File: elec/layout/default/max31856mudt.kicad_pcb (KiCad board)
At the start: 2 copper layers, 225.7 x 100.8 mm, 0 parts

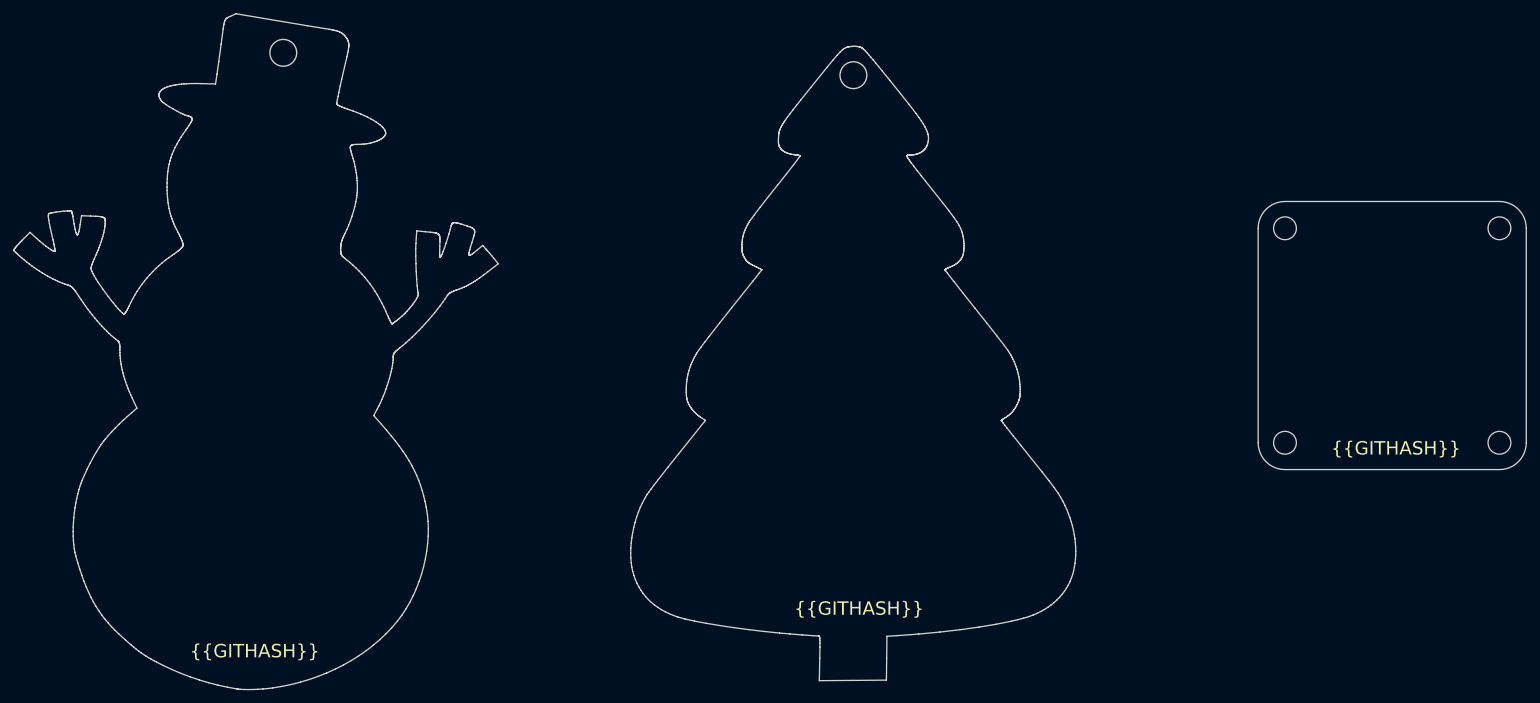
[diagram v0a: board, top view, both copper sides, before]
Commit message: added spi interfaces
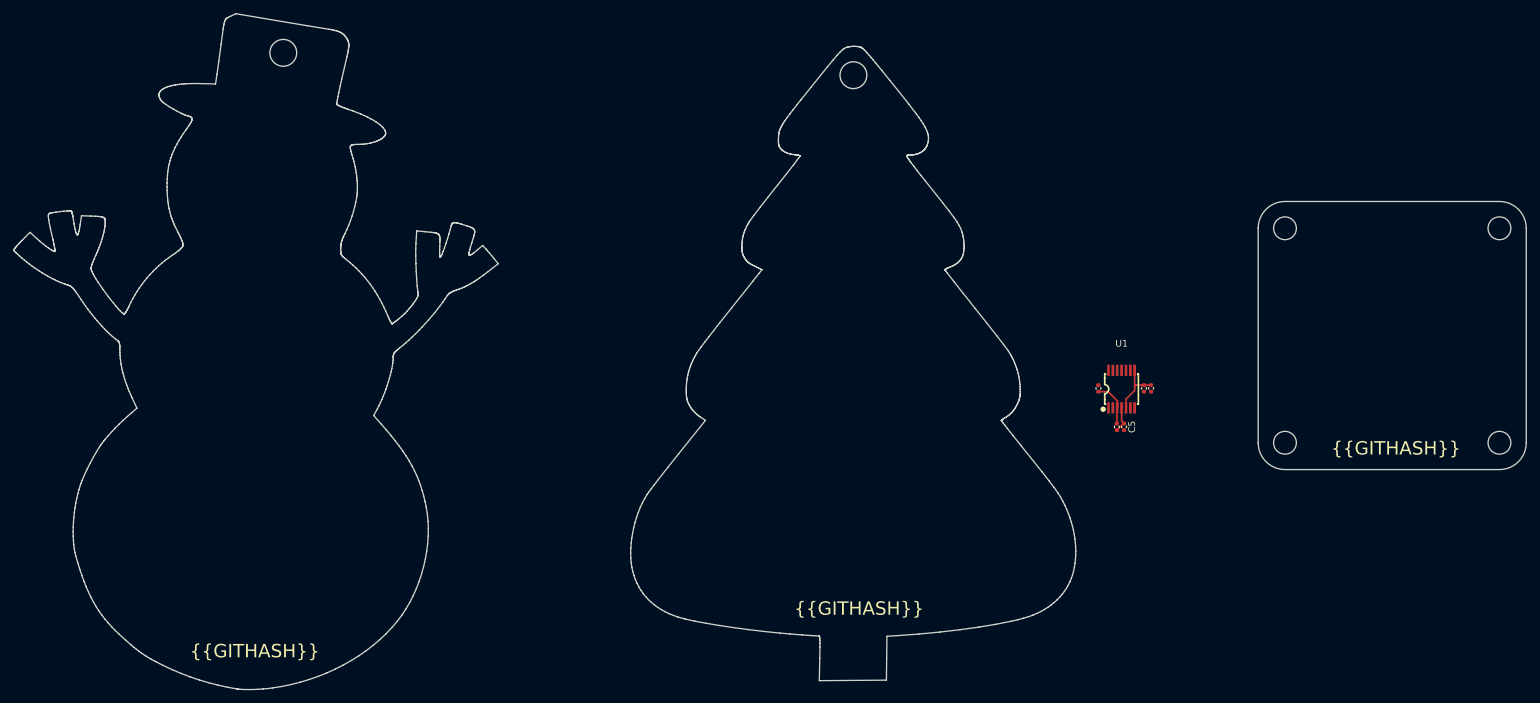
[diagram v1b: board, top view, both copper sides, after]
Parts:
- added C1: Multilayer Ceramic Capacitors MLCC - SMD/SMT 100nF 10V 0402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, lib:C0402, F.Cu at (204.6, 105.7)
- added C2: Multilayer Ceramic Capacitors MLCC - SMD/SMT 100nF 10V 0402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, lib:C0402, F.Cu at (205.6, 105.7)
- added C3: Multilayer Ceramic Capacitors MLCC - SMD/SMT 100nF 10V 0402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, lib:C0402, F.Cu at (200.5, 111.4)
- added C4: Multilayer Ceramic Capacitors MLCC - SMD/SMT 22nF 25V 0402 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, lib:C0402, F.Cu at (197.8, 105.7)
- added C5: Multilayer Ceramic Capacitors MLCC - SMD/SMT 22nF 25V 0402 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, lib:C0402, F.Cu at (201.6, 111.4)
- added U1: , lib:TSSOP-14_L5.0-W4.4-P0.65-LS6.4-BL, F.Cu at (201.2, 105.8)
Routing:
- net vcc-1: track 0.00 -> 8.78 mm
- net vcc: track 0.00 -> 6.81 mm
- net bias: track 0.00 -> 3.99 mm
